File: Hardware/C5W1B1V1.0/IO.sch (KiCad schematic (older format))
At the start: 3 parts, among them J1 Conn_02x20_Counter_Clockwise, J2 Conn_02x20_Counter_Clockwise, J4 Conn_01x04

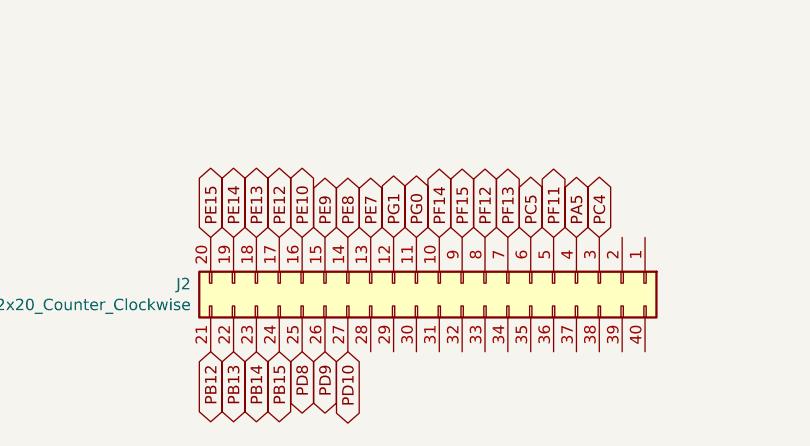
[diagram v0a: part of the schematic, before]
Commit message: Linie PC0-PE13
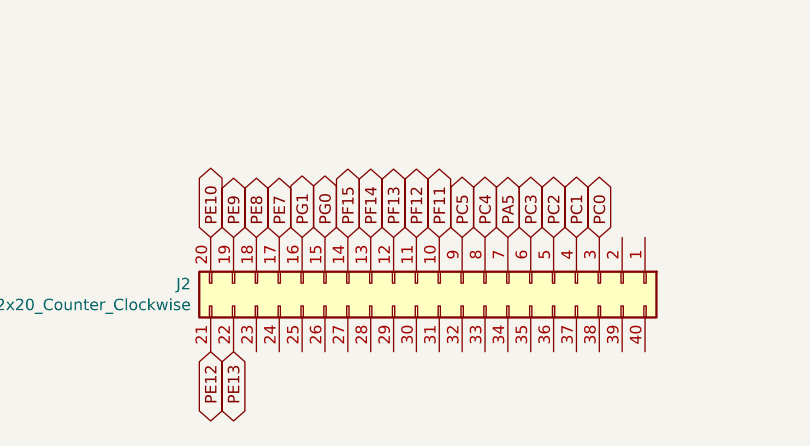
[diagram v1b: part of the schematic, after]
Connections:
- net PB12 is gone; now on net PE12: J2.21 (Pin_21)
- net PB13 is gone; now on net PE13: J2.22 (Pin_22)
- net PE14 is gone; now on net PE9: J2.19 (Pin_19)
- net PE15 is gone; now on net PE10: J2.20 (Pin_20)
- net PA5: now also J2.7 (Pin_7); no longer J2.4 (Pin_4)
- net PC4: now also J2.8 (Pin_8); no longer J2.3 (Pin_3)
- net PC5: now also J2.9 (Pin_9); no longer J2.6 (Pin_6)
- net PE10: no longer J2.16 (Pin_16)
- net PE12: no longer J2.17 (Pin_17)
- net PE13: no longer J2.18 (Pin_18)
- net PE7: now also J2.17 (Pin_17); no longer J2.13 (Pin_13)
- net PE8: now also J2.18 (Pin_18); no longer J2.14 (Pin_14)
- net PE9: no longer J2.15 (Pin_15)
- net PF11: now also J2.10 (Pin_10); no longer J2.5 (Pin_5)
- net PF12: now also J2.11 (Pin_11); no longer J2.8 (Pin_8)
- net PF13: now also J2.12 (Pin_12); no longer J2.7 (Pin_7)
- net PF14: now also J2.13 (Pin_13); no longer J2.10 (Pin_10)
- net PF15: now also J2.14 (Pin_14); no longer J2.9 (Pin_9)
- net PG0: now also J2.15 (Pin_15); no longer J2.11 (Pin_11)
- net PG1: now also J2.16 (Pin_16); no longer J2.12 (Pin_12)
- net PB14: no longer names the net of J2.23 (Pin_23)
- net PB15: no longer names the net of J2.24 (Pin_24)
- net PD10: no longer names the net of J2.27 (Pin_27)
- net PD8: no longer names the net of J2.25 (Pin_25)
- net PD9: no longer names the net of J2.26 (Pin_26)
- new net PC0: J2.3 (Pin_3)
- new net PC1: J2.4 (Pin_4)
- new net PC2: J2.5 (Pin_5)
- new net PC3: J2.6 (Pin_6)
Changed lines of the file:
@@
 	1    0    0    -1
 $EndComp
-Text GLabel 3100 5550 3    50   BiDi ~ 0
-PD10
-Text GLabel 2900 5550 3    50   BiDi ~ 0
-PD8
-Text GLabel 2700 5550 3    50   BiDi ~ 0
-PB14
+Text GLabel 3900 5050 1    50   BiDi ~ 0
+PC3
+Text GLabel 4000 5050 1    50   BiDi ~ 0
+PC2
+Text GLabel 4100 5050 1    50   BiDi ~ 0
+PC1
+Text GLabel 4200 5050 1    50   BiDi ~ 0
+PC0
+Text GLabel 3800 5050 1    50   BiDi ~ 0
+PA5
+Text GLabel 3700 5050 1    50   BiDi ~ 0
+PC4
+Text GLabel 3600 5050 1    50   BiDi ~ 0
+PC5
+Text GLabel 3500 5050 1    50   BiDi ~ 0
+PF11
+Text GLabel 3400 5050 1    50   BiDi ~ 0
+PF12
+Text GLabel 3300 5050 1    50   BiDi ~ 0
+PF13
+Text GLabel 3200 5050 1    50   BiDi ~ 0
+PF14
+Text GLabel 3100 5050 1    50   BiDi ~ 0
+PF15
+Text GLabel 3000 5050 1    50   BiDi ~ 0
+PG0
+Text GLabel 2600 5050 1    50   BiDi ~ 0
+PE9
+Text GLabel 2700 5050 1    50   BiDi ~ 0
+PE8
+Text GLabel 2800 5050 1    50   BiDi ~ 0
+PE7
+Text GLabel 2900 5050 1    50   BiDi ~ 0
+PG1
+Text GLabel 2500 5050 1    50   BiDi ~ 0
+PE10
+Text GLabel 2600 5550 3    50   BiDi ~ 0
+PE13
 Text GLabel 2500 5550 3    50   BiDi ~ 0
-PB12
-Text GLabel 2800 5050 1    50   BiDi ~ 0
 PE12
-Text GLabel 2600 5050 1    50   BiDi ~ 0
-PE14
-Text GLabel 3300 5050 1    50   BiDi ~ 0
-PG1
-Text GLabel 3100 5050 1    50   BiDi ~ 0
-PE8
-Text GLabel 3600 5050 1    50   BiDi ~ 0
-PF15
-Text GLabel 3800 5050 1    50   BiDi ~ 0
-PF13
-Text GLabel 4000 5050 1    50   BiDi ~ 0
-PF11
-Text GLabel 4200 5050 1    50   BiDi ~ 0
-PC4
-Text GLabel 3000 5550 3    50   BiDi ~ 0
-PD9
-Text GLabel 2800 5550 3    50   BiDi ~ 0
-PB15
-Text GLabel 2600 5550 3    50   BiDi ~ 0
-PB13
-Text GLabel 2700 5050 1    50   BiDi ~ 0
-PE13
-Text GLabel 2500 5050 1    50   BiDi ~ 0
-PE15
-Text GLabel 3200 5050 1    50   BiDi ~ 0
-PE7
-Text GLabel 3000 5050 1    50   BiDi ~ 0
-PE9
-Text GLabel 3400 5050 1    50   BiDi ~ 0
-PG0
-Text GLabel 3500 5050 1    50   BiDi ~ 0
-PF14
-Text GLabel 3700 5050 1    50   BiDi ~ 0
-PF12
-Text GLabel 3900 5050 1    50   BiDi ~ 0
-PC5
-Text GLabel 4100 5050 1    50   BiDi ~ 0
-PA5
-Text GLabel 2900 5050 1    50   BiDi ~ 0
-PE10
 $EndSCHEMATC

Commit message: Rozlana masa
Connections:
- net PC0 is gone; now on net +3V3: J2.3 (Pin_3)
- net PC1 is gone; now on net +3V3: J2.4 (Pin_4)
- net GND: now also J1.3 (Pin_3), J1.37 (Pin_37), J1.38 (Pin_38), J1.39 (Pin_39), J1.4 (Pin_4), J1.40 (Pin_40), J2.1 (Pin_1), J2.2 (Pin_2), J2.40 (Pin_40)
- net +12V: now reaches J1.1 (Pin_1)
- net +12V: now also J1.2 (Pin_2)
- net PE0: now reaches J1.10 (Pin_10)
- net PB9: now reaches J1.11 (Pin_11)
- net PB8: now reaches J1.12 (Pin_12)
- net PB7: now reaches J1.13 (Pin_13)
- net PB6: now reaches J1.14 (Pin_14)
- net PB5: now reaches J1.15 (Pin_15)
- net PB4: now reaches J1.16 (Pin_16)
- net PB3: now reaches J1.17 (Pin_17)
- net PG15: now reaches J1.18 (Pin_18)
- net PG14: now reaches J1.19 (Pin_19)
- net PG13: now reaches J1.20 (Pin_20)
- net PD6: now reaches J1.21 (Pin_21)
- net PD5: now reaches J1.22 (Pin_22)
- net PD3: now reaches J1.23 (Pin_23)
- net PD4: now reaches J1.24 (Pin_24)
- net PA15: now reaches J1.25 (Pin_25)
- net PG4: now reaches J1.26 (Pin_26)
- net PK0: now reaches J1.27 (Pin_27)
- net PK1: now reaches J1.28 (Pin_28)
- net PK2: now reaches J1.29 (Pin_29)
- net PG2: now reaches J1.30 (Pin_30)
- net PG3: now reaches J1.31 (Pin_31)
- net +5V: now reaches J1.32 (Pin_32)
- net +5V: now also J1.34 (Pin_34), J2.38 (Pin_38)
- net +3V3: now reaches J1.33 (Pin_33)
- net +3V3: now also J1.35 (Pin_35), J1.36 (Pin_36), J2.39 (Pin_39)
- net PF5: now reaches J1.5 (Pin_5)
- net PF8: now reaches J1.6 (Pin_6)
- net PF9: now reaches J1.7 (Pin_7)
- net PF10: now reaches J1.8 (Pin_8)
- net PE1: now reaches J1.9 (Pin_9)
- net PB13: now reaches J2.23 (Pin_23)
- net PB14: now reaches J2.24 (Pin_24)
- net PB15: now reaches J2.25 (Pin_25)
- net PD8: now reaches J2.26 (Pin_26)
- net PD9: now reaches J2.27 (Pin_27)
- net PD10: now reaches J2.28 (Pin_28)
- net PD11: now reaches J2.29 (Pin_29)
- net PD12: now reaches J2.30 (Pin_30)
- net PD13: now reaches J2.31 (Pin_31)
- net PD14: now reaches J2.32 (Pin_32)
- net PD15: now reaches J2.33 (Pin_33)
- net PJ8: now reaches J2.34 (Pin_34)
- net PJ9: now reaches J2.35 (Pin_35)
- net PJ10: now reaches J2.36 (Pin_36)
- net PJ11: now reaches J2.37 (Pin_37)
